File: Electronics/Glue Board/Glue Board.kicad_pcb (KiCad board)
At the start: 4 copper layers, 10 parts, among them J1 Conn_01x02_Male, J2 Barrel_Jack, Q1 CSD17501Q5A, U1 PCA9685PW, U2 DRV8870DDA, U3 VNH5019A-E, U4 ADS1115IDGS, U5 ISO1540, U6 TPS2121RUXR

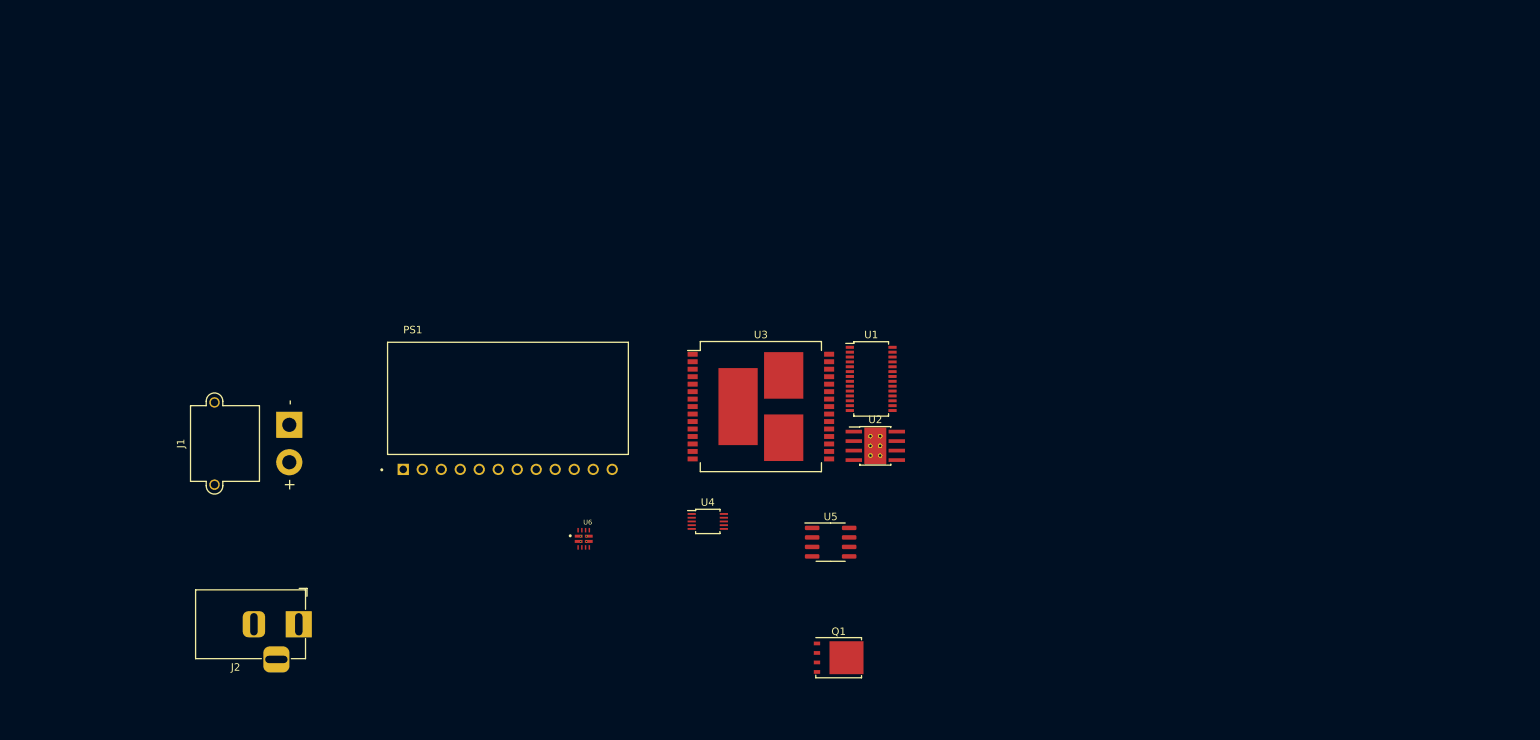
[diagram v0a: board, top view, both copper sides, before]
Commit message: Finished the schematic for the most parts
Finished the schematic for the most parts
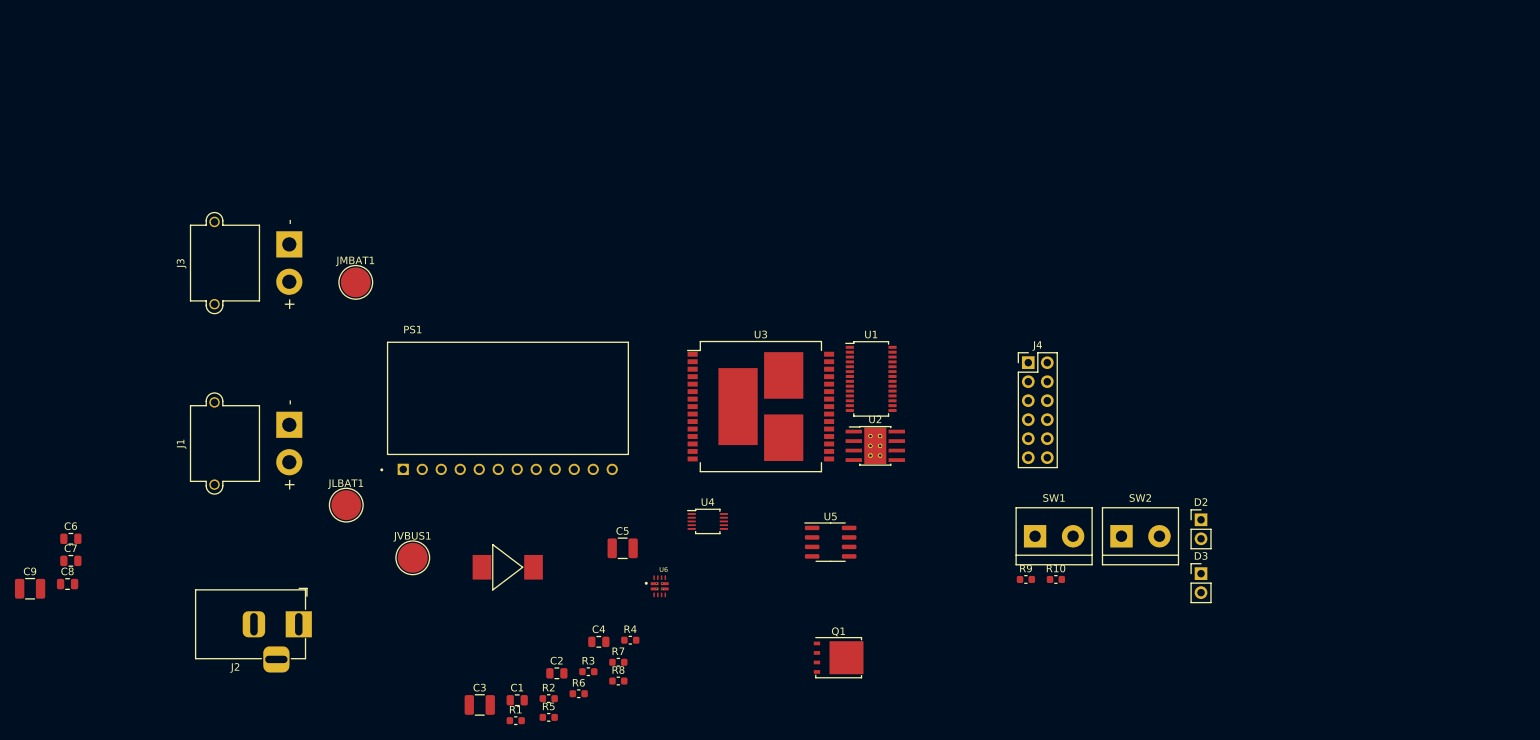
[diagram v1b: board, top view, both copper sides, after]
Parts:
- added C1: 1uF, Capacitor_SMD:C_0805_2012Metric, F.Cu at (114.3, 114.3)
- added C2: 1uF, Capacitor_SMD:C_0805_2012Metric, F.Cu at (119.6, 110.7)
- added C3: 100uF, Capacitor_SMD:C_1210_3225Metric, F.Cu at (109.3, 114.9)
- added C4: 1uF, Capacitor_SMD:C_0805_2012Metric, F.Cu at (125.2, 106.5)
- added C5: 100uF, Capacitor_SMD:C_1210_3225Metric, F.Cu at (128.4, 94.0)
- added C6: 1uF, Capacitor_SMD:C_0805_2012Metric, F.Cu at (54.6, 92.7)
- added C7: 1uF, Capacitor_SMD:C_0805_2012Metric, F.Cu at (54.6, 95.7)
- added C8: 10uF, Capacitor_SMD:C_0805_2012Metric, F.Cu at (54.2, 98.8)
- added C9: 100uF, Capacitor_SMD:C_1210_3225Metric, F.Cu at (49.2, 99.4)
- added D1: STPS5L60S, agg:DO-214AB-SMC, F.Cu at (113.0, 96.5)
- added D2: LED, Connector_PinHeader_2.54mm:PinHeader_1x02_P2.54mm_Vertical, F.Cu at (205.7, 90.2)
- added D3: LED, Connector_PinHeader_2.54mm:PinHeader_1x02_P2.54mm_Vertical, F.Cu at (205.7, 97.4)
- added J3: Conn_01x02_Male, Connector_AMASS:AMASS_XT30PW-M_1x02_P2.50mm_Horizontal, F.Cu at (83.8, 53.3)
- added J4: Conn_02x06_Odd_Even, Connector_PinHeader_2.54mm:PinHeader_2x06_P2.54mm_Vertical, F.Cu at (182.6, 69.2)
- added JLBAT1: TestPoint, TestPoint:TestPoint_Pad_D4.0mm, F.Cu at (91.4, 88.2)
- added JMBAT1: TestPoint, TestPoint:TestPoint_Pad_D4.0mm, F.Cu at (92.7, 58.4)
- added JVBUS1: TestPoint, TestPoint:TestPoint_Pad_D4.0mm, F.Cu at (100.3, 95.2)
- added R1: 23.7k, Resistor_SMD:R_0603_1608Metric, F.Cu at (114.1, 117.0)
- added R10: 470, Resistor_SMD:R_0603_1608Metric, F.Cu at (186.3, 98.2)
- added R2: 5k, Resistor_SMD:R_0603_1608Metric, F.Cu at (118.5, 114.1)
- added R3: 2.6k, Resistor_SMD:R_0603_1608Metric, F.Cu at (123.8, 110.5)
- added R4: 10.2k, Resistor_SMD:R_0603_1608Metric, F.Cu at (129.4, 106.3)
- added R5: 5k, Resistor_SMD:R_0603_1608Metric, F.Cu at (118.5, 116.6)
- added R6: 23.7k, Resistor_SMD:R_0603_1608Metric, F.Cu at (122.5, 113.4)
- added R7: 5k, Resistor_SMD:R_0603_1608Metric, F.Cu at (127.8, 109.2)
- added R8: 18.7k, Resistor_SMD:R_0603_1608Metric, F.Cu at (127.8, 111.7)
- added R9: 47R, Resistor_SMD:R_0603_1608Metric, F.Cu at (182.3, 98.2)
- added SW1: SW_SPST, TerminalBlock:TerminalBlock_bornier-2_P5.08mm, F.Cu at (183.6, 92.4)
- added SW2: SW_SPST, TerminalBlock:TerminalBlock_bornier-2_P5.08mm, F.Cu at (195.1, 92.4)
- moved U6 12.0 mm to (133.3, 99.1)
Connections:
- J1 pad 1: Net-(J1-Pad1) -> GND
- J1 pad 2: Net-(J1-Pad2) -> Net-(C2-Pad1)
- J2 pad 1: Net-(J2-Pad1) -> Net-(C1-Pad1)
- J2 pad 2: Net-(J2-Pad2) -> GND
- PS1 pad 2: Net-(PS1-Pad2) -> Net-(C2-Pad1)
- PS1 pad 3: Net-(PS1-Pad2) -> Net-(C2-Pad1)
- PS1 pad 4: Net-(PS1-Pad2) -> Net-(C2-Pad1)
- PS1 pad 5: Net-(PS1-Pad5) -> GND
- PS1 pad 6: Net-(PS1-Pad5) -> GND
- PS1 pad 7: Net-(PS1-Pad5) -> GND
- PS1 pad 8: Net-(PS1-Pad5) -> GND
- Q1 pad 1: Net-(Q1-Pad1) -> VBUS
- Q1 pad 2: Net-(Q1-Pad1) -> VBUS
- Q1 pad 3: Net-(Q1-Pad1) -> VBUS
- Q1 pad 5: Net-(Q1-Pad5) -> VCC
- U3 pad 11: Net-(U3-Pad11) -> Net-(Q1-Pad4)
- U3 pad 12: Net-(U3-Pad12) -> VBUS
- U3 pad 13: Net-(U3-Pad13) -> VCC
- U3 pad 23: Net-(U3-Pad13) -> VCC
- U3 pad 3: Net-(U3-Pad13) -> VCC
- U3 pad 31: Net-(U3-Pad13) -> VCC
- U6 pad 12: Net-(U6-Pad12) -> GND
- U6 pad 3: Net-(U6-Pad3) -> GND
- U6 pad 7: Net-(U6-Pad7) -> Net-(C1-Pad1)
- U6 pad 7_1: Net-(U6-Pad7) -> Net-(C1-Pad1)
- U6 pad 9: Net-(U6-Pad9) -> GND

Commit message: Complete Schematic and BOM
Complete Schematic and BOM. Next up, layout!
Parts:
- added C10: 0.1uF, Capacitor_SMD:C_0805_2012Metric, F.Cu at (136.9, 33.1)
- added C11: 33nF, Capacitor_SMD:C_0805_2012Metric, F.Cu at (133.1, 37.1)
- added C12: 0.1uF, Capacitor_SMD:C_0805_2012Metric, F.Cu at (127.5, 40.5)
- added C13: 22uF, Capacitor_SMD:C_0805_2012Metric, F.Cu at (147.0, 25.3)
- added C14: 0.1uF, Capacitor_SMD:C_0805_2012Metric, F.Cu at (131.9, 40.5)
- added C15: 47uF, Capacitor_SMD:C_0805_2012Metric, F.Cu at (141.3, 33.1)
- added C16: 0.1uF, Capacitor_SMD:C_0805_2012Metric, F.Cu at (137.5, 36.1)
- added C17: 1uF, Capacitor_SMD:C_0805_2012Metric, F.Cu at (132.1, 47.1)
- added D4: LED_Dual_2pin, LED_SMD:LED_1206_3216Metric, F.Cu at (128.1, 37.4)
- added J5: Conn_01x02_Male, Connector_JST:JST_XH_B2B-XH-AM_1x02_P2.50mm_Vertical, F.Cu at (138.8, 27.2)
- added J6: Conn_01x05_Female, Connector_Molex:Molex_PicoBlade_53047-0510_1x05_P1.25mm_Vertical, F.Cu at (127.8, 26.9)
- added J7: Conn_01x04_Female, Connector_PinHeader_2.54mm:PinHeader_1x04_P2.54mm_Vertical, F.Cu at (127.6, 47.9)
- added R11: 10k, Resistor_SMD:R_0603_1608Metric, F.Cu at (151.2, 25.1)
- added R12: 10k, Resistor_SMD:R_0603_1608Metric, F.Cu at (137.3, 38.8)
- added R13: 10k, Resistor_SMD:R_0603_1608Metric, F.Cu at (145.5, 32.9)
- added R14: 220, Resistor_SMD:R_0603_1608Metric, F.Cu at (141.7, 35.9)
- added R15: 220, Resistor_SMD:R_0603_1608Metric, F.Cu at (136.1, 41.3)
- added R16: 220, Resistor_SMD:R_0603_1608Metric, F.Cu at (151.2, 27.6)
- added R17: 220, Resistor_SMD:R_0603_1608Metric, F.Cu at (155.2, 25.1)
- added R18: 220, Resistor_SMD:R_0603_1608Metric, F.Cu at (141.7, 38.4)
- added R19: 10k, Resistor_SMD:R_0603_1608Metric, F.Cu at (149.5, 32.1)
- added R20: 1k, Resistor_SMD:R_0603_1608Metric, F.Cu at (140.1, 41.3)
- added R21: 1k, Resistor_SMD:R_0603_1608Metric, F.Cu at (145.7, 35.4)
- added R22: 1k, Resistor_SMD:R_0603_1608Metric, F.Cu at (155.2, 27.6)
- added R23: 1k, Resistor_SMD:R_0603_1608Metric, F.Cu at (145.7, 37.9)
- added R24: 1k, Resistor_SMD:R_0603_1608Metric, F.Cu at (153.5, 30.1)
- added R25: 4.7k, Resistor_SMD:R_0603_1608Metric, F.Cu at (149.7, 34.6)
- added R26: 10k, Resistor_SMD:R_0603_1608Metric, F.Cu at (144.1, 40.9)
- added R27: 4.7k, Resistor_SMD:R_0603_1608Metric, F.Cu at (149.7, 37.1)
- added R28: 1k, Resistor_SMD:R_0603_1608Metric, F.Cu at (153.8, 32.7)
- added R29: 30K, Resistor_SMD:R_0603_1608Metric, F.Cu at (148.1, 40.5)
- added R30: 4.7k, Resistor_SMD:R_0603_1608Metric, F.Cu at (153.8, 35.2)
- added R31: 10k, Resistor_SMD:R_0603_1608Metric, F.Cu at (136.3, 46.9)
- added R32: 10k, Resistor_SMD:R_0603_1608Metric, F.Cu at (136.3, 49.4)
- added R33: 10k, Resistor_SMD:R_0603_1608Metric, F.Cu at (131.9, 49.8)
- added TP1: TestPoint, TestPoint:TestPoint_Pad_D2.0mm, F.Cu at (146.8, 28.8)
- added U2: DRV8871DDA, Package_SO:Texas_HTSOP-8-1EP_3.9x4.9mm_P1.27mm_EP2.95x4.9mm_Mask2.4x3.1mm_ThermalVias, F.Cu at (130.0, 32.4)
- U3: value VNH5019A-E -> VNH5019ATR-E
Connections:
- U1 pad 1: Net-(U1-Pad1) -> GND
- U1 pad 14: Net-(U1-Pad14) -> GND
- U1 pad 2: Net-(U1-Pad2) -> GND
- U1 pad 24: Net-(U1-Pad24) -> GND
- U1 pad 25: Net-(U1-Pad25) -> GND
- U1 pad 26: Net-(U1-Pad26) -> SCL
- U1 pad 27: Net-(U1-Pad27) -> SDA
- U1 pad 28: Net-(U1-Pad28) -> +5V
- U1 pad 3: Net-(U1-Pad3) -> GND
- U1 pad 4: Net-(U1-Pad4) -> GND
- U1 pad 5: Net-(U1-Pad5) -> GND
- U3 pad 18: Net-(U3-Pad18) -> GND
- U3 pad 19: Net-(U3-Pad18) -> GND
- U3 pad 20: Net-(U3-Pad18) -> GND
- U3 pad 26: Net-(U3-Pad26) -> GND
- U3 pad 27: Net-(U3-Pad26) -> GND
- U3 pad 28: Net-(U3-Pad26) -> GND
- U4 pad 1: Net-(U4-Pad1) -> GND
- U4 pad 10: Net-(U4-Pad10) -> SCL
- U4 pad 3: Net-(U4-Pad3) -> GND
- U4 pad 4: Net-(U4-Pad4) -> STEERING_POS_ADC
- U4 pad 5: Net-(U4-Pad5) -> DRIVE_CS_ADC
- U4 pad 8: Net-(U4-Pad8) -> +5V
- U4 pad 9: Net-(U4-Pad9) -> SDA

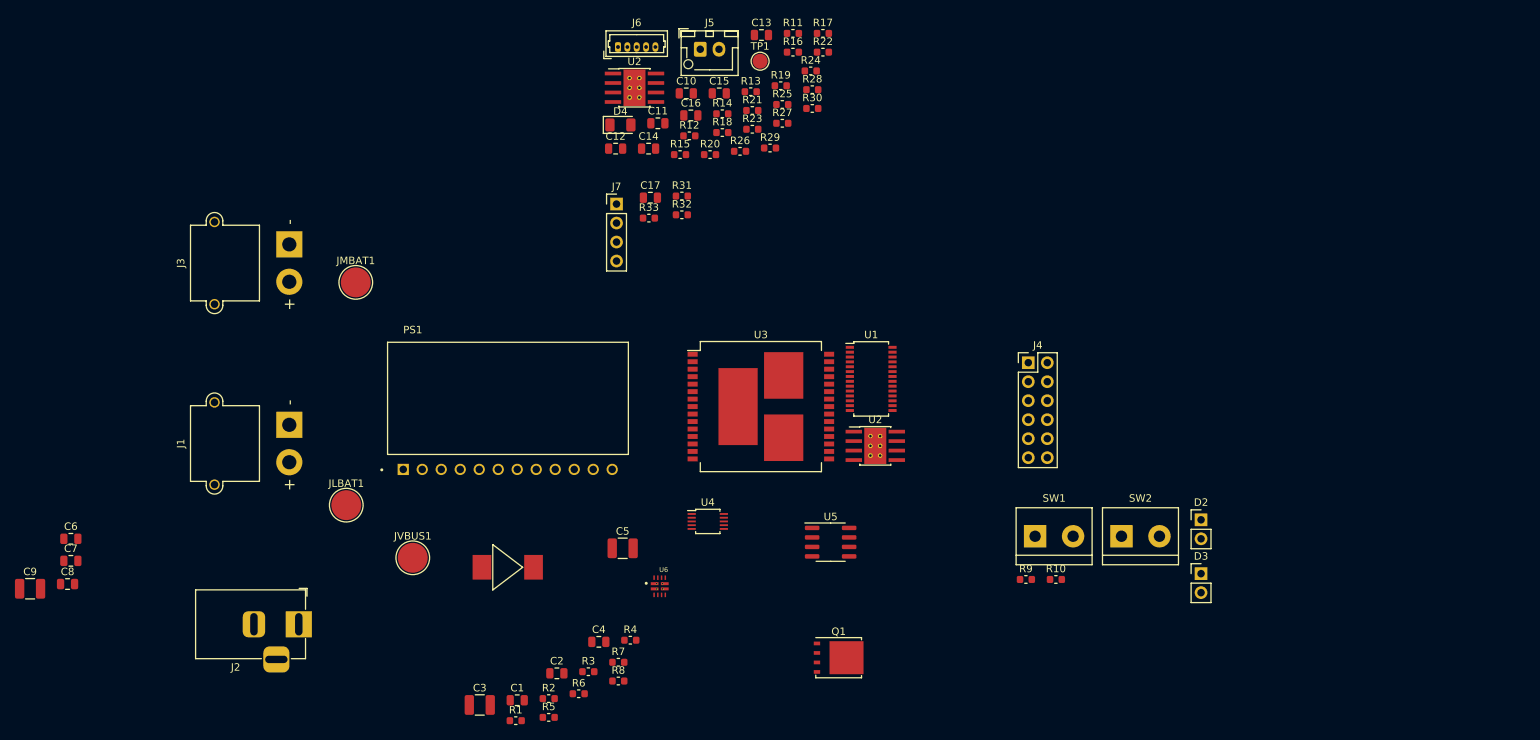
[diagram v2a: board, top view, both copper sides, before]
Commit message: Added Motor v-sense and battery mon. Layout time!
Added Motor v-sense and battery mon. Layout time!
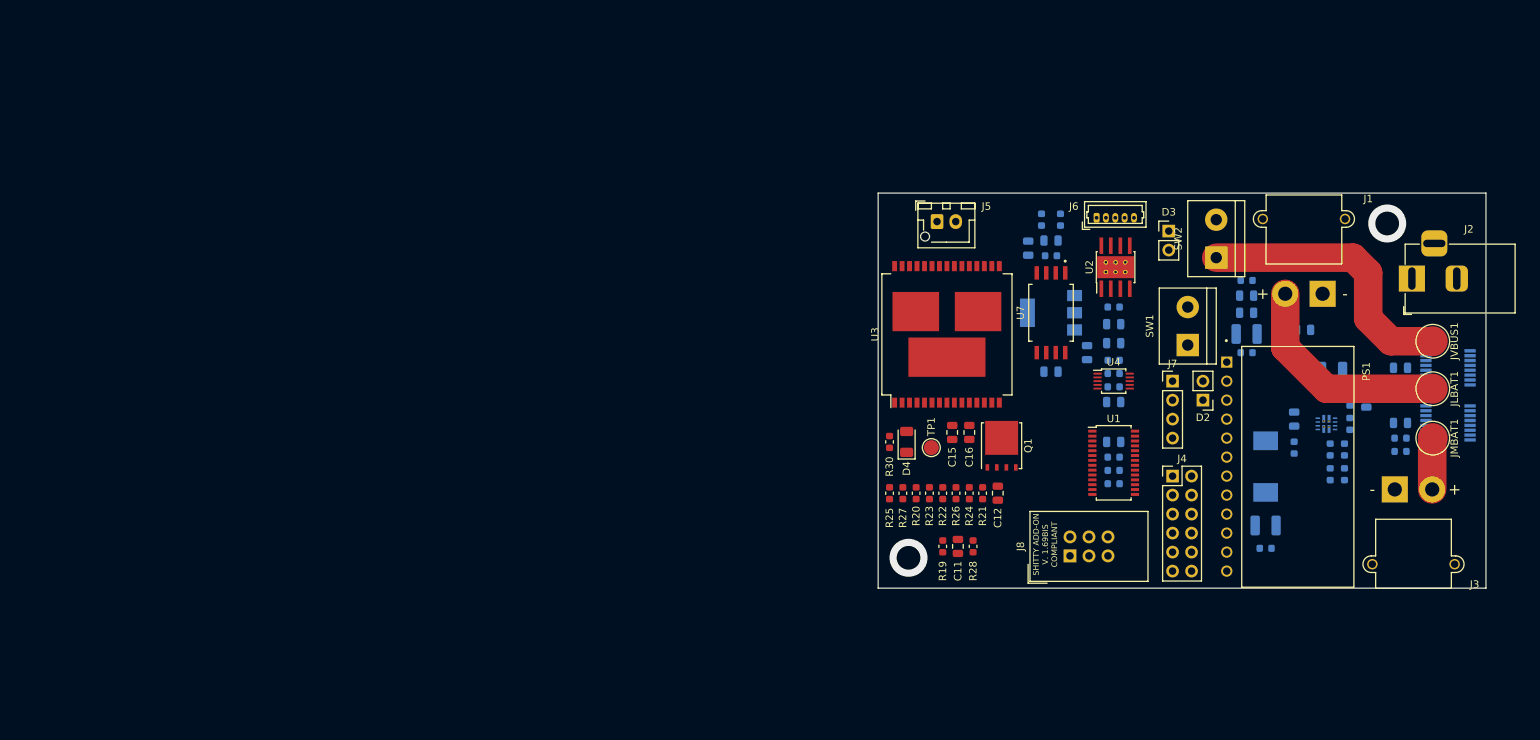
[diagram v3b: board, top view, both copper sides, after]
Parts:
- removed R14, R15, R16, R17, R18: 220, Resistor_SMD:R_0603_1608Metric
- removed the U2 at (130.0, 32.4)
- removed the U2 at (162.2, 80.3)
- added C18: 33nF, Capacitor_SMD:C_0805_2012Metric, B.Cu at (185.7, 52.8)
- added C19: 10uF, Capacitor_SMD:C_0805_2012Metric, B.Cu at (190.5, 67.8)
- added C20: 10uF, Capacitor_SMD:C_0805_2012Metric, B.Cu at (182.6, 53.8)
- added C21: 33nF, Capacitor_SMD:C_0805_2012Metric, B.Cu at (185.7, 70.4)
- added C22: 1uF, Capacitor_SMD:C_0805_2012Metric, B.Cu at (232.4, 69.8)
- added C23: 1uF, Capacitor_SMD:C_0805_2012Metric, B.Cu at (232.4, 77.2)
- added J8: Conn_02x03_Odd_Even, Connector_IDC:IDC-Header_2x03_P2.54mm_Vertical, F.Cu at (188.2, 95.0)
- added R34: 10k, Resistor_SMD:R_0603_1608Metric, B.Cu at (186.9, 50.0)
- added R35: 470R, Resistor_SMD:R_0603_1608Metric, B.Cu at (185.7, 54.9)
- added R36: 10k, Resistor_SMD:R_0603_1608Metric, B.Cu at (184.4, 50.0)
- added R37: 10k, Resistor_SMD:R_0603_1608Metric, B.Cu at (232.4, 71.9)
- added R38: 10k, Resistor_SMD:R_0603_1608Metric, B.Cu at (232.4, 79.2)
- added R39: 10k, Resistor_SMD:R_0603_1608Metric, B.Cu at (232.4, 73.7)
- added R40: 10k, Resistor_SMD:R_0603_1608Metric, B.Cu at (232.4, 81.0)
- added U2: DRV8871DDA, Package_SO:Texas_HTSOP-8-1EP_3.9x4.9mm_P1.27mm_EP2.95x4.9mm_Mask2.4x3.1mm_ThermalVias, F.Cu at (194.3, 56.4)
- added U7: AMC1301DWVR, libs:SOIC127P1150X280-8N, F.Cu at (185.7, 62.5)
- added U8: INA260, Package_SO:TSSOP-16_4.4x5mm_P0.65mm, B.Cu at (238.8, 69.8)
- added U9: INA260, Package_SO:TSSOP-16_4.4x5mm_P0.65mm, B.Cu at (238.8, 77.2)
- C1, C10, C13, C14, C17, C2, C3, C4, C5, C6, C7, C8, C9, D1, R1, R10, R11, R12, R13, R2, R29, R3, R31, R32, R33, R4, R5, R6, R7, R8, R9, U6: moved to B.Cu
- J7: value Conn_01x04_Female -> Conn_01x04_Male
- U5: value ISO1540 -> NCP1117-5.0_SOT223; footprint Package_SO:SOIC-8_3.9x4.9mm_P1.27mm -> Package_TO_SOT_SMD:SOT-223-3_TabPin2; moved to B.Cu
- moved C6 179.8 mm to (232.4, 66.0), turned to 180 degrees
- moved C9 166.2 mm to (211.8, 65.3), turned to 180 degrees
- moved C8 161.8 mm to (211.8, 62.5), turned to 180 degrees
- moved C7 161.2 mm to (211.8, 60.2), turned to 180 degrees
- moved J2 155.9 mm to (233.9, 57.9), turned to 180 degrees
- moved J3 151.4 mm to (231.6, 86.1), turned to 180 degrees
- moved JLBAT1 146.1 mm to (236.7, 72.6), turned to 270 degrees
- moved JMBAT1 145.5 mm to (236.7, 79.2), turned to 270 degrees
- moved JVBUS1 139.4 mm to (236.7, 66.3), turned to 270 degrees
- moved J1 139.3 mm to (222.0, 59.9), turned to 0 degrees
- moved C1 120.4 mm to (227.8, 74.2), turned to 270 degrees
- moved R1 114.8 mm to (223.0, 80.8), turned to 270 degrees
- moved R5 111.3 mm to (224.9, 84.1), turned to 270 degrees
- moved R6 110.4 mm to (225.6, 74.1), turned to 270 degrees
- moved C2 109.9 mm to (219.5, 64.8)
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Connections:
- net Net-(C2-Pad1) renamed VLOGIC_BAT
- net Net-(C6-Pad1) renamed VMOTOR_BAT
- D4 pad 2: Net-(D4-Pad2) -> OUTA
- J4 pad 1: Net-(J4-Pad1) -> +3.3V
- J5 pad 1: Net-(J5-Pad1) -> OUTA
- J5 pad 2: Net-(D4-Pad2) -> OUTB
- J7 pad 1: GND -> +5V
- J7 pad 2: Net-(J7-Pad2) -> GND
- J7 pad 3: GND -> SDA
- J7 pad 4: Net-(J7-Pad4) -> SCL
- R30 pad 2: Net-(J5-Pad1) -> OUTB
- U1 pad 10: Net-(R18-Pad2) -> IN2
- U1 pad 6: Net-(R14-Pad2) -> INA
- U1 pad 7: Net-(R15-Pad2) -> INB
- U1 pad 8: Net-(R16-Pad2) -> DRIVE_PWM
- U1 pad 9: Net-(R17-Pad2) -> IN1
- U3 pad 1: Net-(D4-Pad2) -> OUTA
- U3 pad 15: Net-(J5-Pad1) -> OUTB
- U3 pad 16: Net-(J5-Pad1) -> OUTB
- U3 pad 21: Net-(J5-Pad1) -> OUTB
- U3 pad 25: Net-(D4-Pad2) -> OUTA
- U3 pad 30: Net-(D4-Pad2) -> OUTA
- U3 pad 32: Net-(J5-Pad1) -> OUTB
- U3 pad 33: Net-(D4-Pad2) -> OUTA
- U4 pad 6: Net-(J7-Pad4) -> VMOTOR_P_ADC
- U4 pad 7: Net-(J7-Pad2) -> VMOTOR_N_ADC
- U5 pad 1: Net-(U5-Pad1) -> GND
- U5 pad 2: Net-(U5-Pad2) -> +5VA
- U5 pad 3: Net-(U5-Pad3) -> VBUS
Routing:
- net Net-(C7-Pad1): track 0.00 -> 37.2 mm
- net VLOGIC_BAT: track 0.00 -> 29.2 mm
- net VMOTOR_BAT: track 0.00 -> 6.89 mm
- net (no net): vias 0 -> 2
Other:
- board outline added: 81.3 x 52.8 mm
- board text added: "SHITTY ADD-ON V. 1.69BIS COMPLIANT"
